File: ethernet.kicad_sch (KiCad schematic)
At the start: 33 parts, among them J200 RJ45_Hanrun_HR911105A_Horizon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, U200 LAN8742A, U201 USBLC6-4SC6, Y200 25MHz

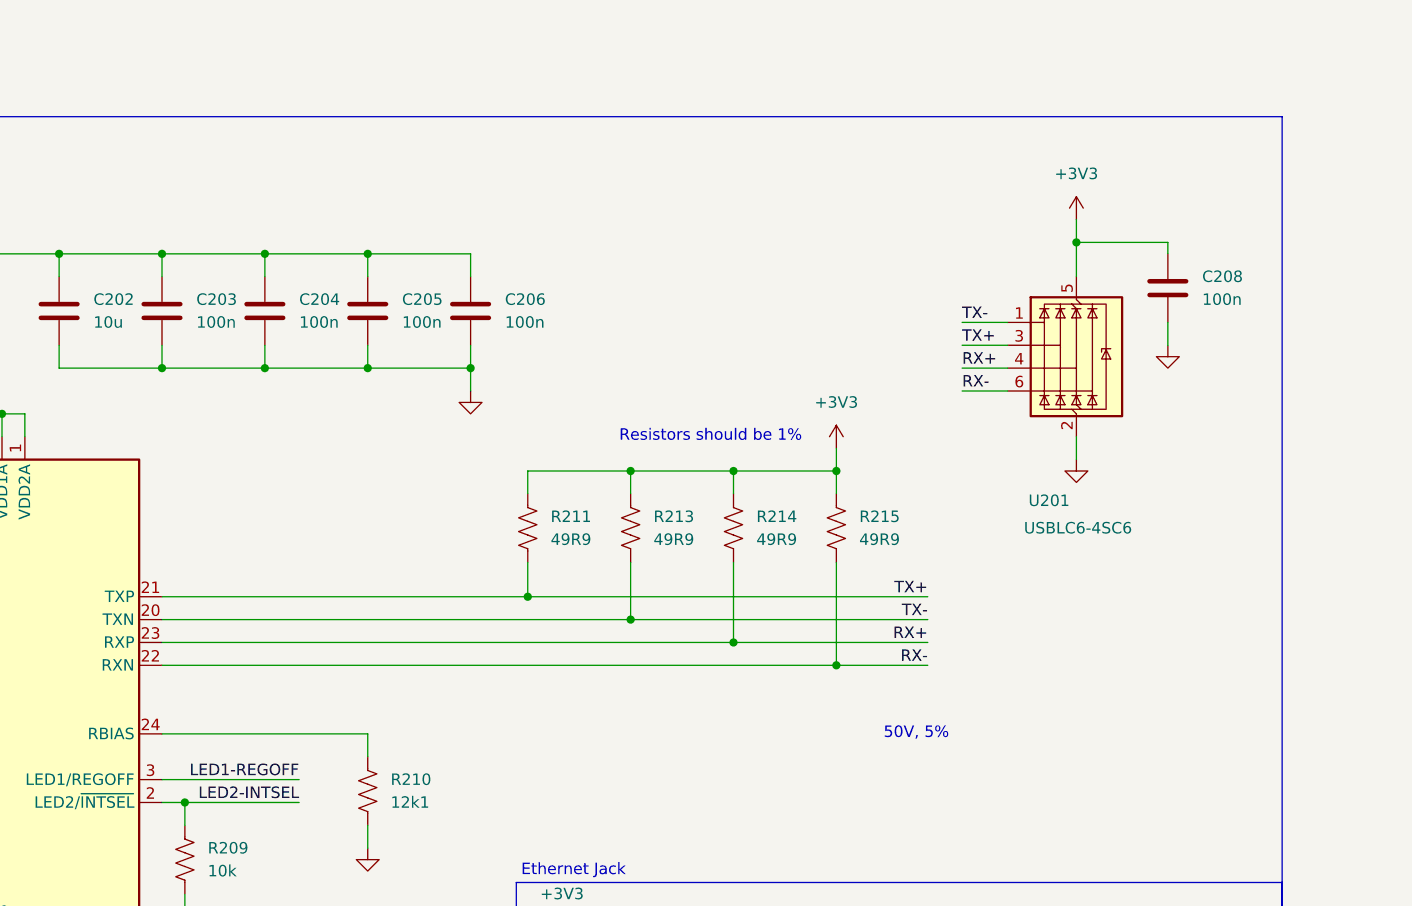
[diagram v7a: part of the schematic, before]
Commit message: Swap to ESD204 for ethernet to enable better routing
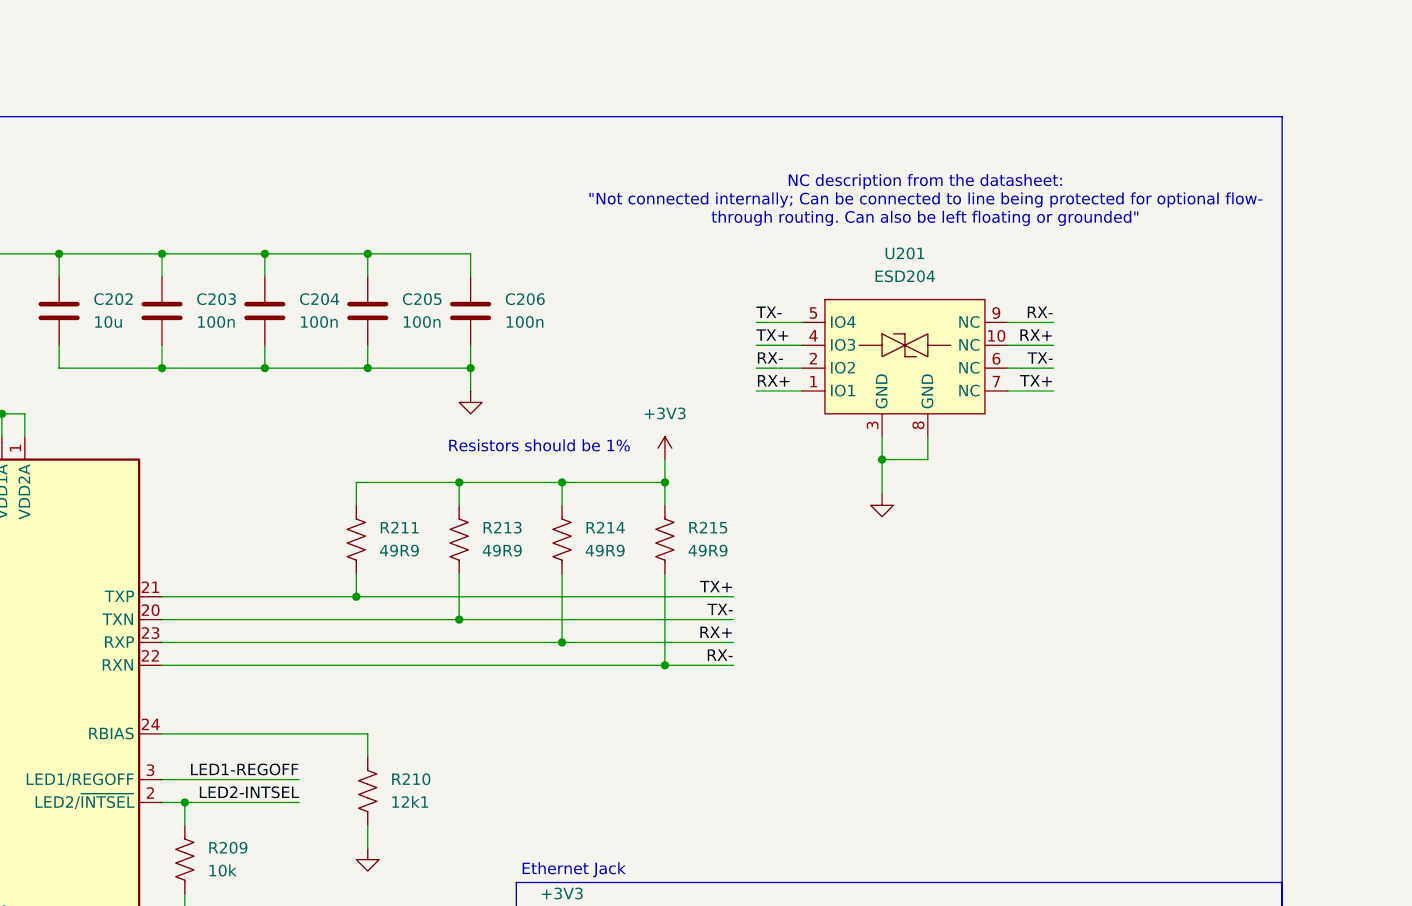
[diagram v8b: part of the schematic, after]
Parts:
- removed C208: 100n, Capacitor_SMD:C_0402_1005Metric, symbol Device:C
- removed U201: USBLC6-4SC6, Package_TO_SOT_SMD:SOT-23-6, symbol Power_Protection:USBLC6-4SC6
- added U201: ESD204, Package_DFN_QFN:Diodes_UDFN-10_1.0x2.5mm_P0.5mm, symbol customlib:ESD204
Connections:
- net GND: now also U201.3 (GND), U201.8 (GND)
- net RX+: now also U201.1 (IO1), U201.10 (NC)
- net RX-: now also U201.2 (IO2), U201.9 (NC)
- net TX+: now also U201.4 (IO3), U201.7 (NC)
- net TX-: now also U201.5 (IO4), U201.6 (NC)
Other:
- note added: "NC description from the datasheet: "Not connected internally; Can be connected to line being protected for optional flow- through routing. Can also be left floating or grounded""
- note removed: "50V, 5%"
- moved on the sheet: R211, R213, R214, R215
